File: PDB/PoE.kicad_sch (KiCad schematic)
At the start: 35 parts, among them J13 RJ45_Abracon_ARJP11A-MASA-B-A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, Q5 CSD19502Q5B, Q6 CSD19502Q5B, U14 LM5118MH, U15 INA228

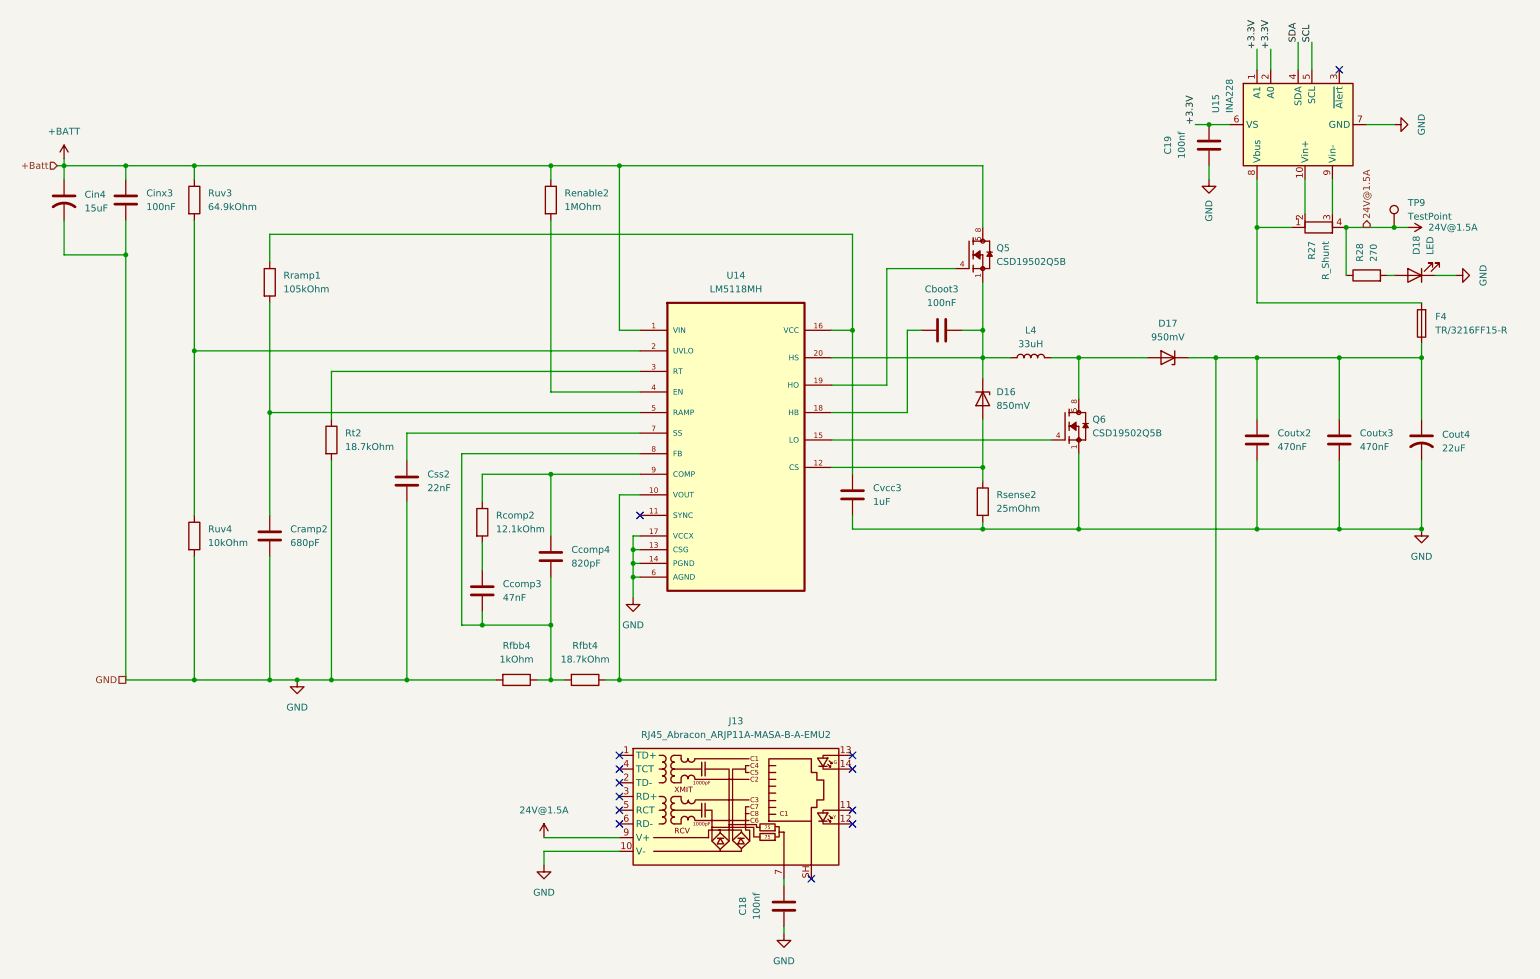
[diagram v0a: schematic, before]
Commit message: PoE+
Swap 24V for 48V and most of PoE+ controller is added with footprints for ic added
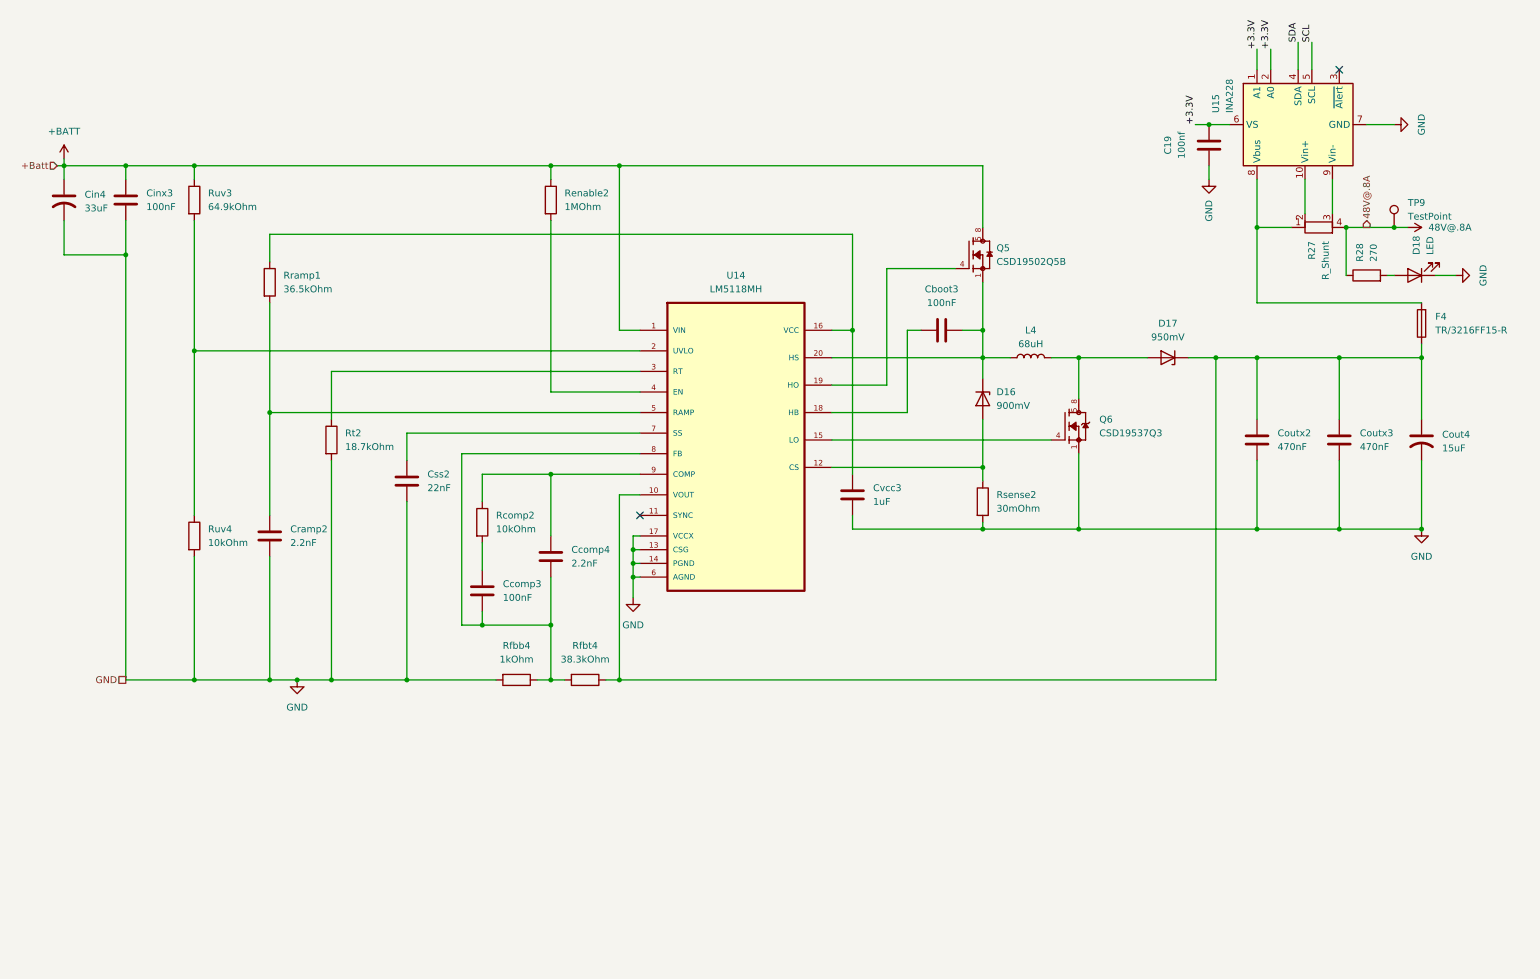
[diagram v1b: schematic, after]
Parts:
- removed C18: 100nf, Capacitor_SMD:C_0603_1608Metric, symbol Device:C
- removed J13: RJ45_Abracon_ARJP11A-MASA-B-A-EMU2, Connector_RJ:RJ45_Abracon_ARJP11A-MA_Horizontal, symbol Connector:RJ45_Abracon_ARJP11A-MASA-B-A-EMU2
- removed Q6: CSD19502Q5B, Dependencies:CSD19502Q5B, symbol sym&foot:CSD19502Q5B
- added Q6: CSD19537Q3, foot:CSD19537Q3, symbol sym&foot:CSD19537Q3
- Ccomp3: value 47nF -> 100nF
- Ccomp4: value 820pF -> 2.2nF
- Cin4: value 15uF -> 33uF
- Cout4: value 22uF -> 15uF
- Cramp2: value 680pF -> 2.2nF
- D16: value 850mV -> 900mV
- L4: value 33uH -> 68uH
- Rcomp2: value 12.1kOhm -> 10kOhm
- Rfbt4: value 18.7kOhm -> 38.3kOhm
- Rramp1: value 105kOhm -> 36.5kOhm
- Rsense2: value 25mOhm -> 30mOhm
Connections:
- net GND: now also Q6.1, Q6.2, Q6.3
- net at D17.2 (A), L4.2: now also Q6.5_8
- net at U14.15 (LO): now also Q6.4
- net 24V@1.5A renamed 48V@.8A
- no-connect marks 13 -> 2

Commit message: laid out many, many things
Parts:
- R27: footprint Resistor_SMD:R_Shunt_Vishay_WSR2_WSR3_KelvinConnection -> Resistor_SMD:R_Shunt_Vishay_WSK2512_6332Metric_T2.66mm
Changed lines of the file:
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@@
 			)
 		)
-		(property "Footprint" "Resistor_SMD:R_Shunt_Vishay_WSR2_WSR3_KelvinConnection"
+		(property "Footprint" "Resistor_SMD:R_Shunt_Vishay_WSK2512_6332Metric_T2.66mm"
 			(at 252.73 58.928 90)
 			(hide yes)

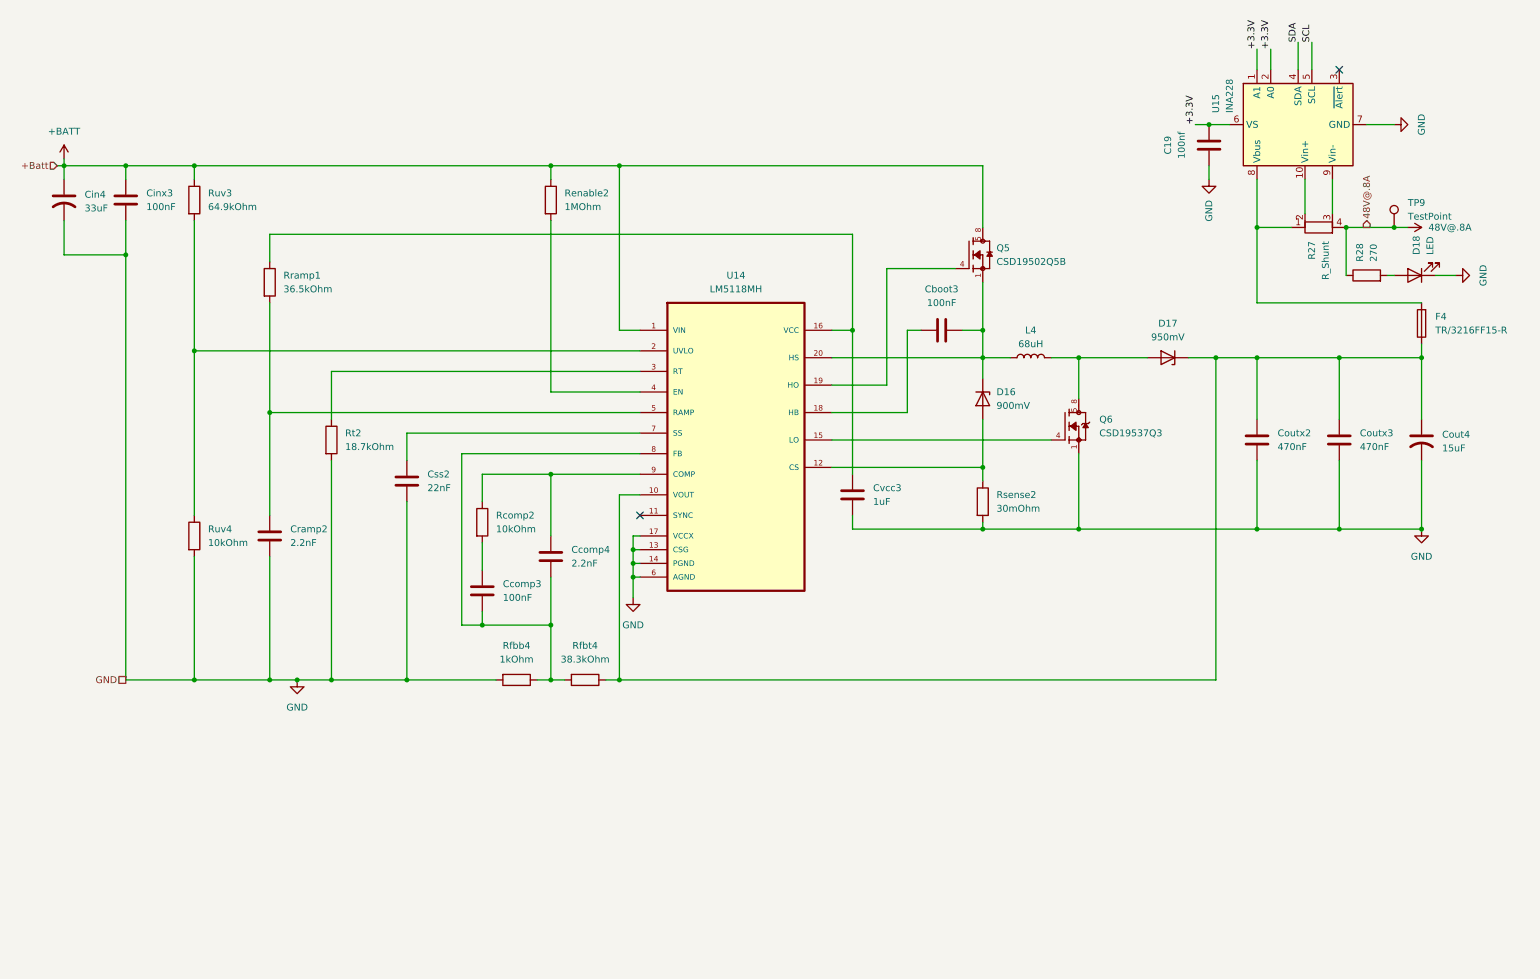
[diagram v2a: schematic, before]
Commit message: coordinated labels in schem
Labeled all components to be Rxx, Cxx, ext forms through all sheets so labels for BOM and layout are work together as one long list.
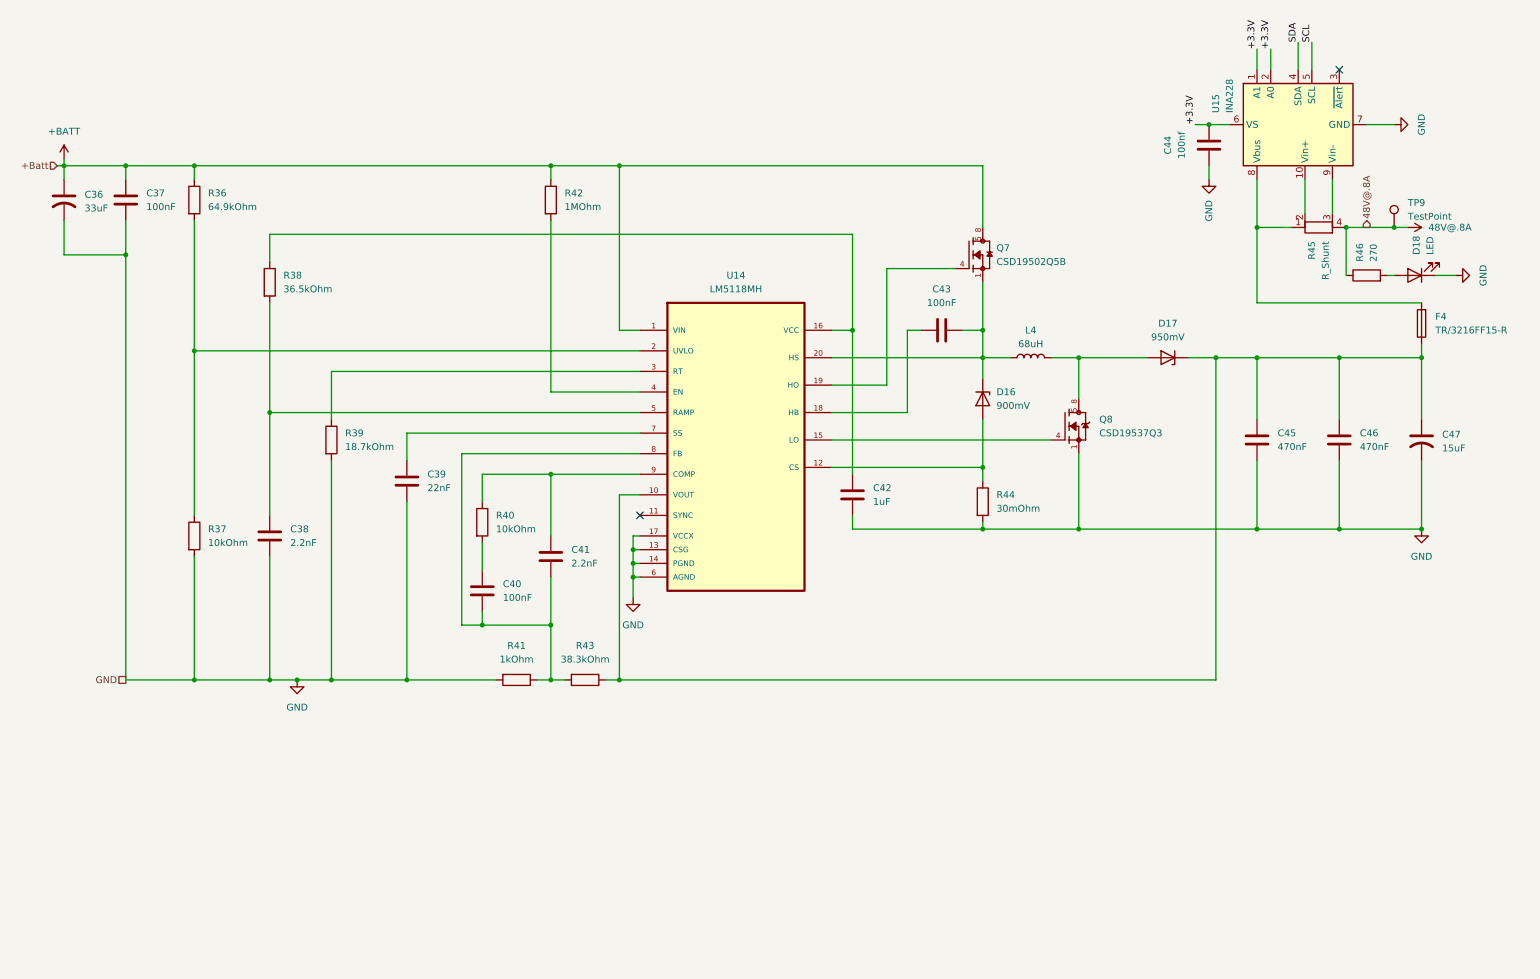
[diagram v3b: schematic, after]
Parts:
- renumbered Cin4 to C36, Cinx3 to C37, Cramp2 to C38, Css2 to C39, Ccomp3 to C40, Ccomp4 to C41, Cvcc3 to C42, Cboot3 to C43, C19 to C44, Coutx2 to C45, Coutx3 to C46, Cout4 to C47, Q5 to Q7, Q6 to Q8, Ruv3 to R36, Ruv4 to R37, Rramp1 to R38, Rt2 to R39, Rcomp2 to R40, Rfbb4 to R41, Renable2 to R42, Rfbt4 to R43, Rsense2 to R44, R27 to R45, R28 to R46

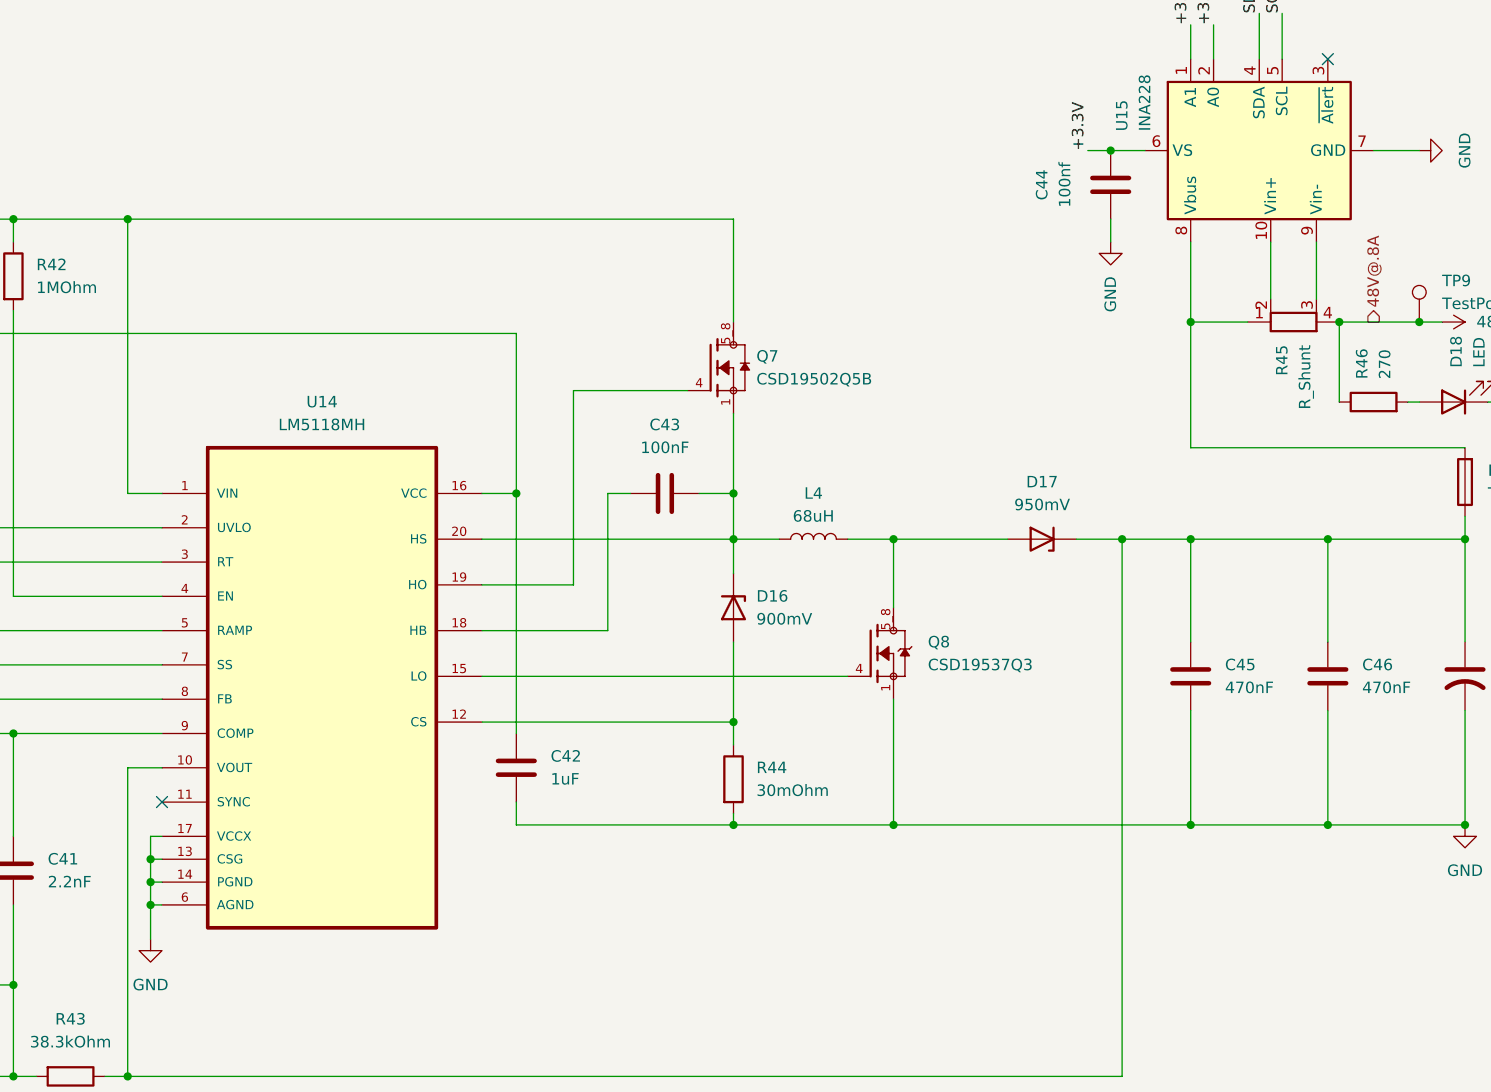
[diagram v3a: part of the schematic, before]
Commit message: last push before removing oring
i think we're going with an interlock system instead. the battery oring on here will take far too much physical room on the board to make it worthwhile. this push removes the oring and assumes a single power input.
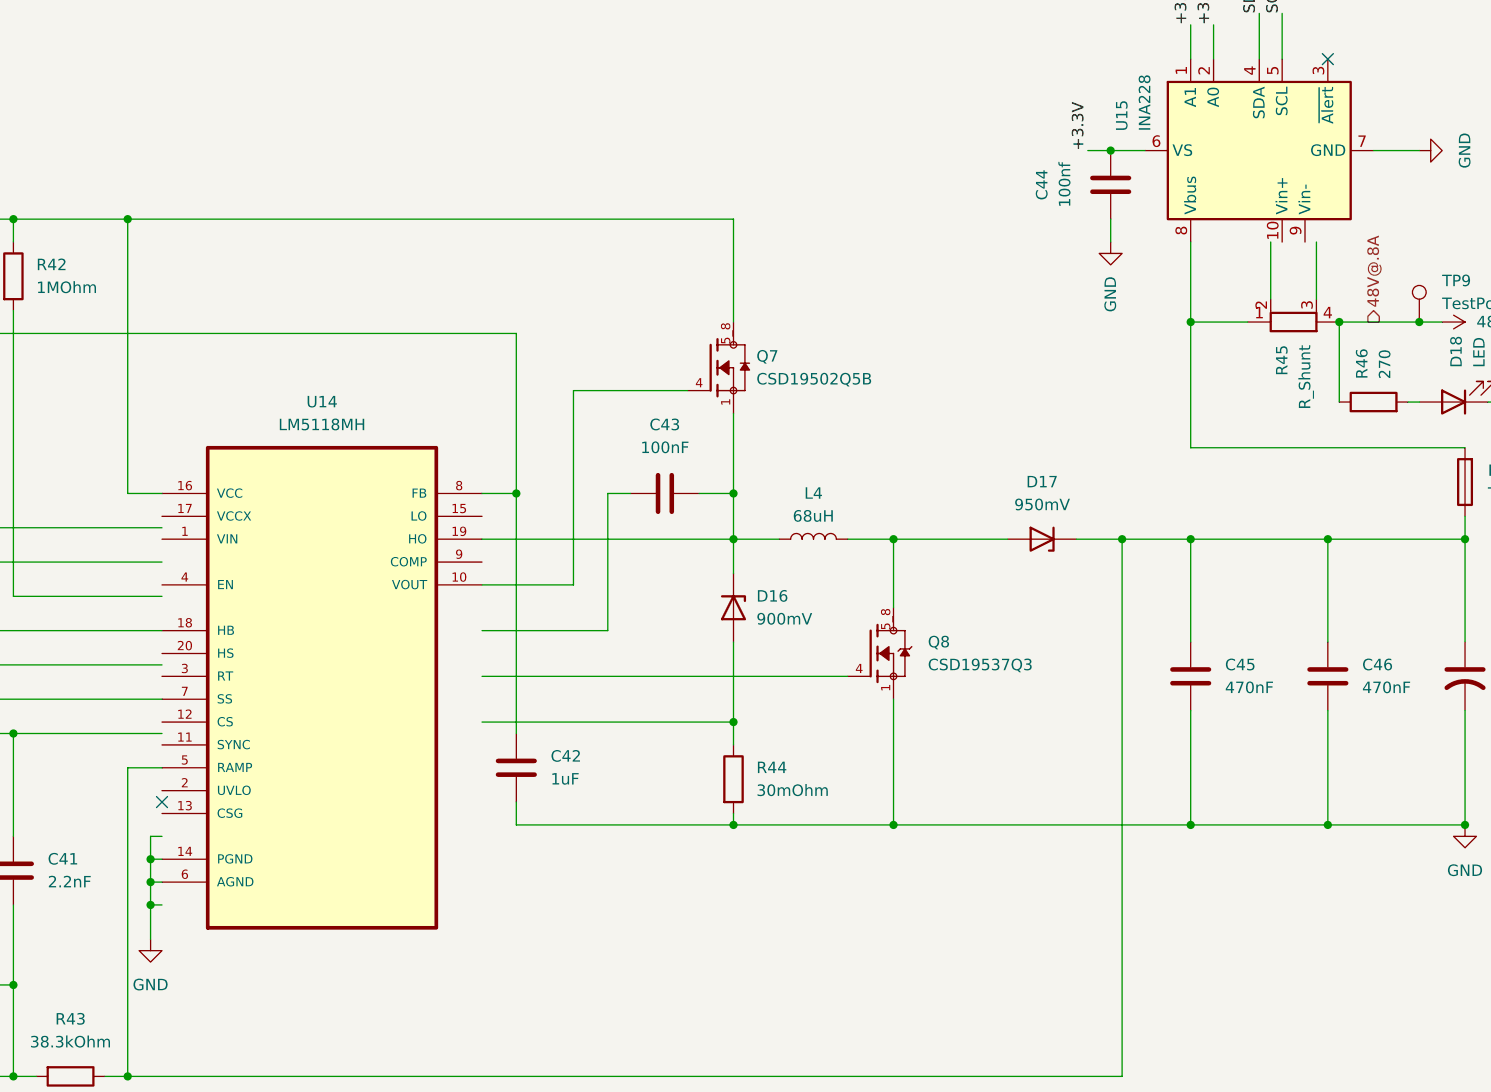
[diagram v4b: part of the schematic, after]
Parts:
- Q7: footprint Dependencies:CSD19502Q5B -> CSD19502Q5B:TRANS_CSD19502Q5B
- Q8: footprint foot:CSD19537Q3 -> CSD19537Q3:TRANS_CSD19537Q3
- U14: footprint Dependencies:LM5118MH -> LM5118MH:SOP65P640X110-21N
- U15: footprint Package_SO:HVSSOP-10-1EP_3x3mm_P0.5mm_EP1.83x1.89mm -> Package_SO:TSSOP-10_3x3mm_P0.5mm
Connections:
- net +BATT: now also U14.16 (VCC); no longer U14.1 (VIN)
- net GND: no longer U14.13 (CSG), U14.17 (VCCX)
- net at C43.1, D16.1 (K), L4.1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: now also U14.19 (HO); no longer U14.20 (HS)
- net at C40.2, C41.2, R41.1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: now also U14.7 (SS); no longer U14.8 (FB)
- net at C45.1, C46.1, C47.1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: now also U14.5 (RAMP); no longer U14.10 (VOUT)
- net at C41.1, R40.1: no longer U14.9 (COMP)
- net at R36.2, R37.1: no longer U14.2 (UVLO)
- net at D16.2 (A), R44.1: no longer U14.12 (CS)
- net at U14.15 (LO): no longer Q8.4
- net at C42.1, R38.1: now also U14.8 (FB); no longer U14.16 (VCC)
- net at U14.18 (HB): now also C38.1, R38.2; no longer C43.2
- net at Q7.4: now also U14.10 (VOUT); no longer U14.19 (HO)
- net at U14.3 (RT): no longer R39.1
- net at U14.4 (EN): no longer R42.2
- net at C39.1: no longer U14.7 (SS)
- net at R45.2: no longer U15.10 (Vin+)
- net at R45.3: no longer U15.9 (Vin-)
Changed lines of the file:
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@@
 			)
 		)
-		(property "Footprint" "Dependencies:LM5118MH"
+		(property "Footprint" "LM5118MH:SOP65P640X110-21N"
 			(at 144.78 93.98 0)
 			(hide yes)
@@
 			)
 		)
-		(property "Footprint" "Package_SO:HVSSOP-10-1EP_3x3mm_P0.5mm_EP1.83x1.89mm"
+		(property "Footprint" "Package_SO:TSSOP-10_3x3mm_P0.5mm"
 			(at 226.314 13.208 0)
 			(hide yes)
@@
 			)
 		)
-		(property "Footprint" "Dependencies:CSD19502Q5B"
+		(property "Footprint" "CSD19502Q5B:TRANS_CSD19502Q5B"
 			(at 190.5 62.23 0)
 			(hide yes)
@@
 			)
 		)
-		(property "Footprint" "foot:CSD19537Q3"
+		(property "Footprint" "CSD19537Q3:TRANS_CSD19537Q3"
 			(at 205.74 93.98 0)
 			(hide yes)
